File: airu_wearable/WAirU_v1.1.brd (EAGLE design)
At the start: 43.8 x 51.7 mm, 53 parts, among them J2 2p-2.0, Q2 MMBT3904LT1G, Q3 MMBT3904LT1G, Q4 BSS84, Q6 BSS84, U2 CN3065-DFN8, U3 HDC1080DMBT, U4 CJT1117-3.3-SOT223, U6 PAM2401, U7 ESP32_WROOM32_SKINNY

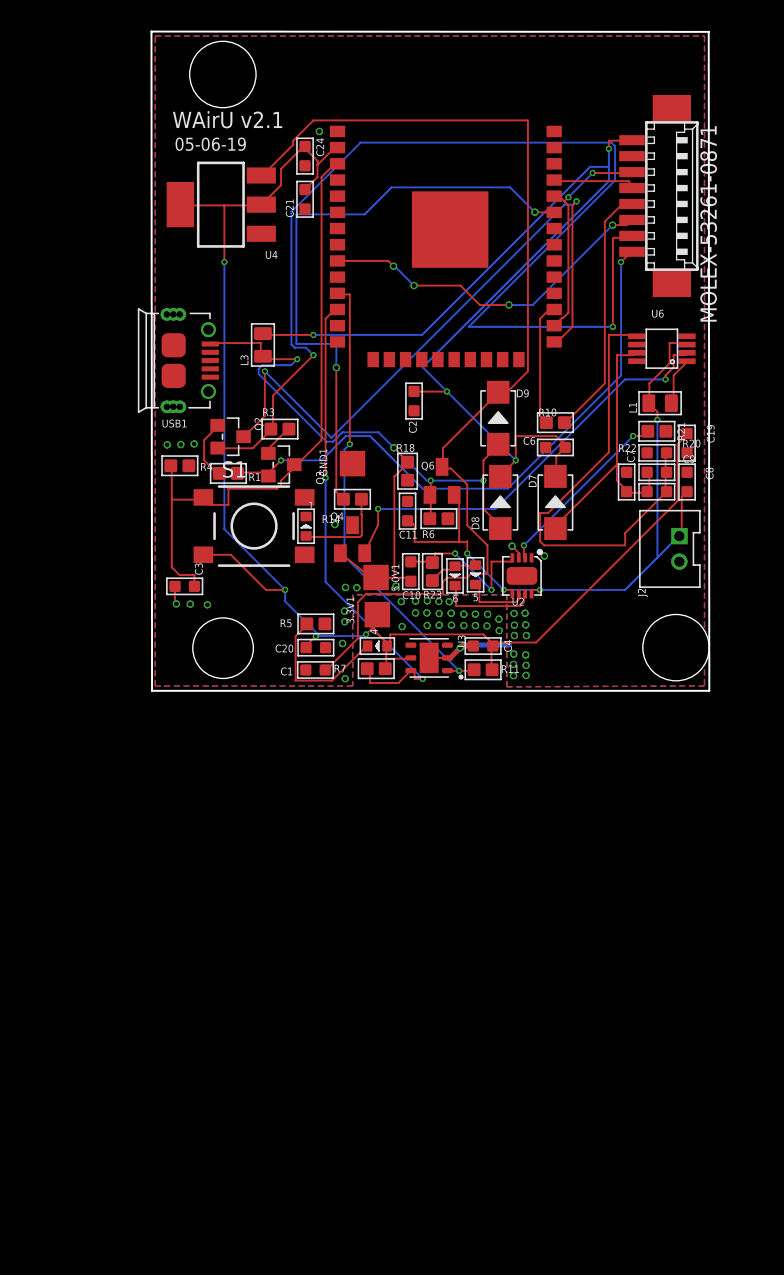
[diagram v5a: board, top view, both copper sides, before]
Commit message: Change regulator, add rules for pads and vias, update new component to BOM sheet
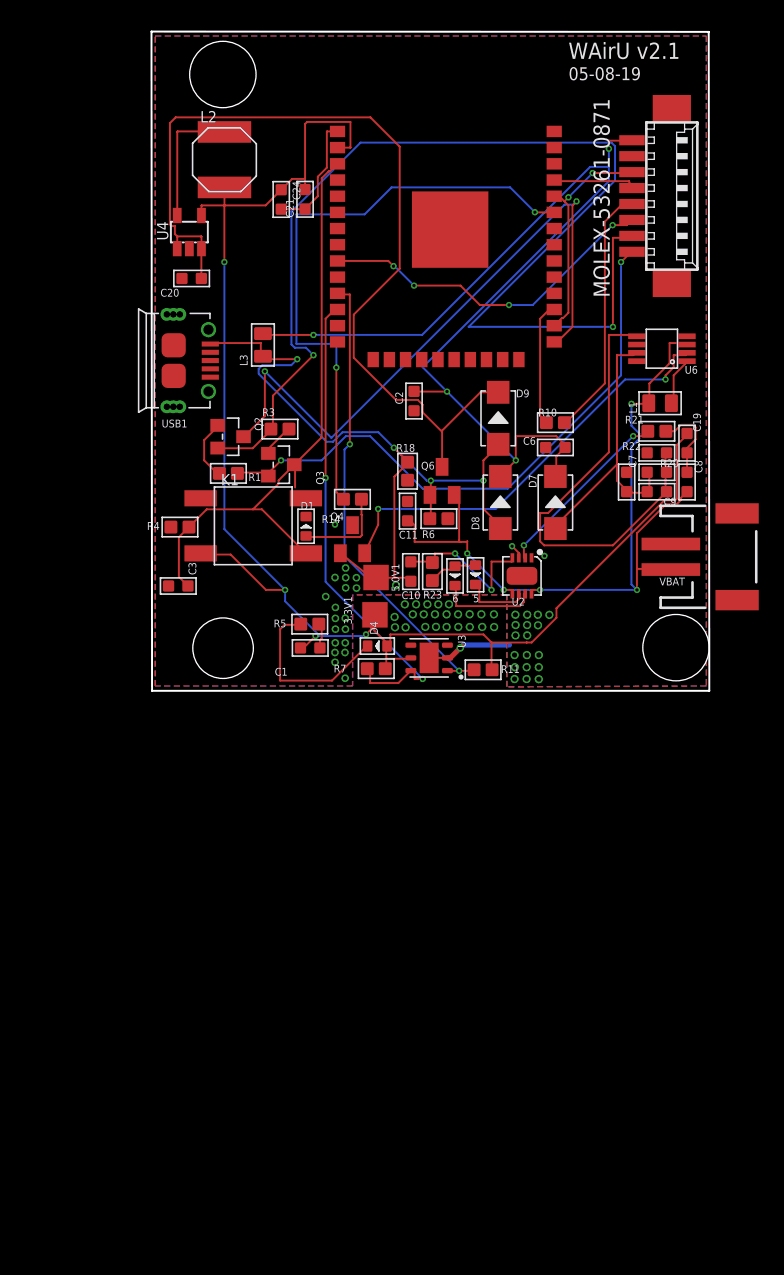
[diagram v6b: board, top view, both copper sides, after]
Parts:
- removed C4: 1uf, Seeed-Capacitor:C0603
- removed GND1: TPTP20SQ, testpad:TP20SQ
- removed J2: 2p-2.0, Seeed-Connector:H2-2.0-6X4.5MM
- removed S1: DTSM-6, switch-tact:DTSM-6
- added K1: (no value), OPL_Switch:SW4-SMD-6.0X6.0X5.0MM
- added L2: 4.7uH, OPL_Inductor:L5040S
- added VBAT: (no value), SparkFun-Connectors:JST-2-SMD
- U4: value CJT1117-3.3-SOT223 -> PAM2305AABADJ; device Seeed-IC:SOT-223 -> OPL_IC:SOT-23-5
- moved C20 32.2 mm to (11.1, 30.8)
- moved R4 4.81 mm to (10.2, 11.3), turned to 90 degrees
- moved C24 3.88 mm to (18.1, 37.0)
- moved U4 3.28 mm to (10.9, 34.4), turned to 0 degrees
- moved C3 0.51 mm to (10.0, 6.66)
- moved R5 0.48 mm to (20.4, 3.66)
- moved C1 0.44 mm to (20.4, 1.80)
- moved 3.3V1 0.19 mm to (25.5, 4.39)
- renumbered 1 to D1, 4 to D4
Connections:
- new net N$75: C20.2, D9.2, Q6.3, U4.1, U4.3
- net 3.3V: now also K1.2, L2.2, U4.4; no longer C4.2, S1.3, U4.2, U4.TER
- net GND: now also U4.2, VBAT.1; no longer C4.1, GND1.TP, J2.-, U4.1
- net N$8: now also L2.1, U4.5; no longer C20.2, D9.2, Q6.3, U4.3
- net RESET: now also K1.3; no longer S1.1
- net VBAT: now also VBAT.2; no longer J2.+
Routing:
- net N$8: track 81.5 -> 10.3 mm
- net N$75: track 0.00 -> 70.8 mm
- net GND: track 10.4 -> 26.3 mm, vias 11 -> 4
- net VBAT: track 55.4 -> 63.5 mm, vias 4 -> 5
- net 3.3V: track 113.2 -> 118.7 mm
- net N$21: track 11.6 -> 14.2 mm
- net N$10: track 36.5 -> 35.9 mm
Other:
- board text added: "05-08-19"
- board text removed: "05-06-19"

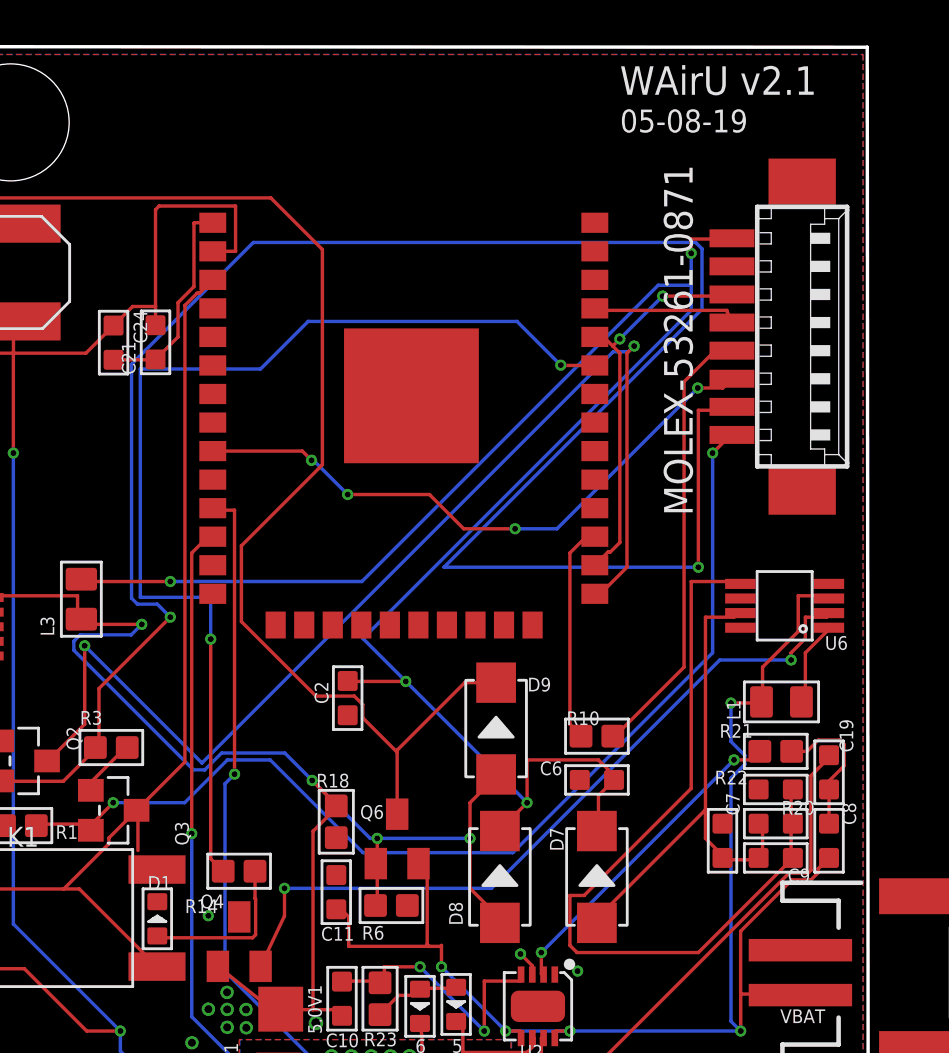
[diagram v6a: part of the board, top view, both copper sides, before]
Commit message: Pull down PM_SET and PM_RESET
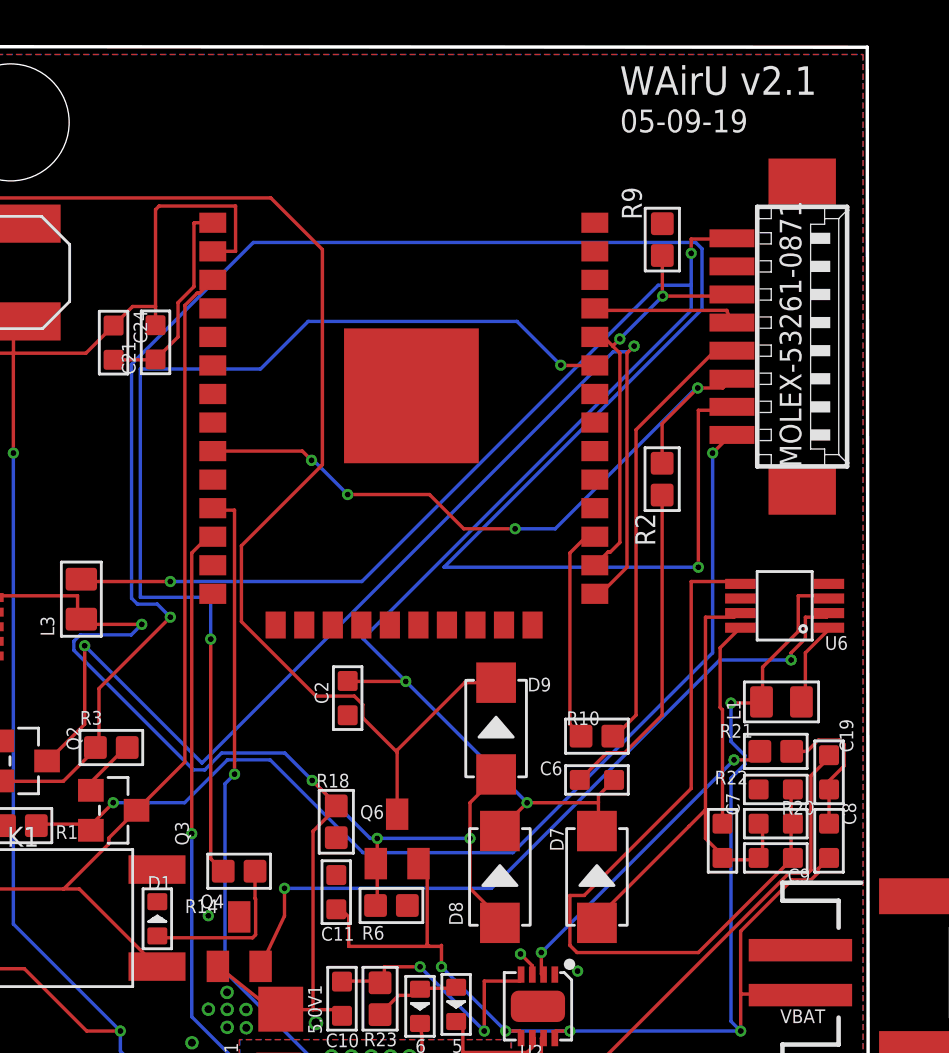
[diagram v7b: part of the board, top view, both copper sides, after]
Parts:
- added R2, R9: 4.7K, Seeed-Resistor:R0603
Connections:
- net GND: now also R2.1, R9.1
- net PM_RESET: now also R2.2
- net PM_SET: now also R9.2
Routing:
- net GND: track 26.3 -> 50.1 mm
- net PM_RESET: track 27.3 -> 31.3 mm
- net 5.0V: track 81.8 -> 79.0 mm
- net RESET: track 48.2 -> 46.3 mm
- net PM_SET: track 17.8 -> 19.6 mm
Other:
- board text added: "05-09-19"
- board text removed: "05-08-19"

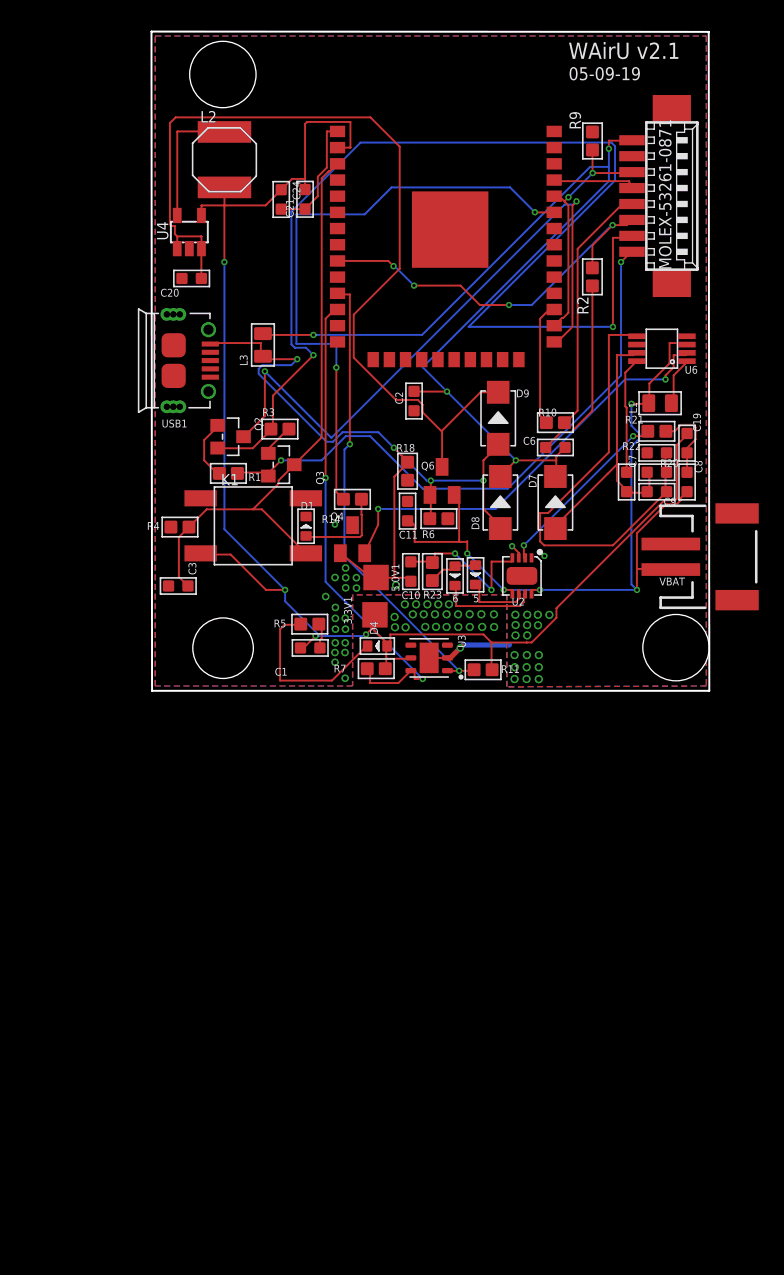
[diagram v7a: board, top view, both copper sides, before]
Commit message: replaced LEDs with single LED, 5V and 3.3V buck/boost are now on the same VIN
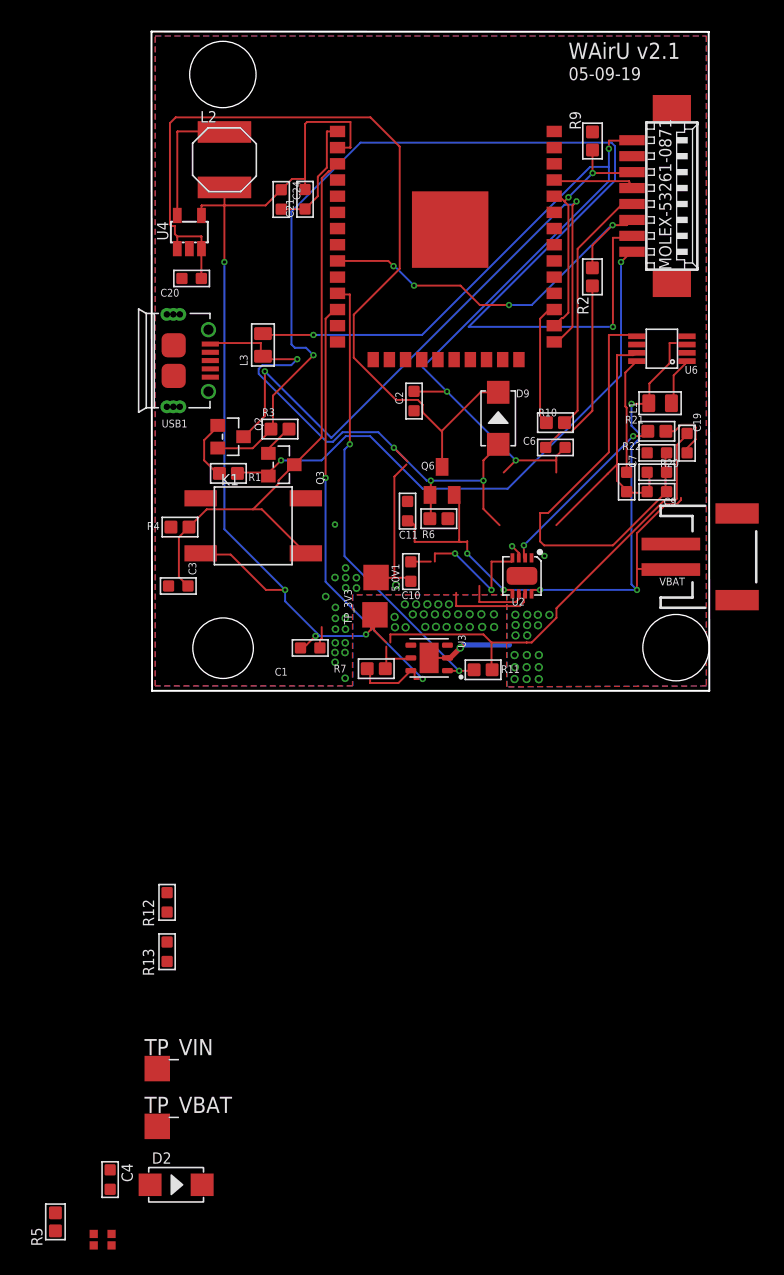
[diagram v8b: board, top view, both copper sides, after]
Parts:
- removed 5: GREEN-0603, Seeed-LED:LED-0603
- removed 6, D1: RED-0603, Seeed-LED:LED-0603
- removed C8: 10uf, OPL_Capacitor:C0603
- removed D4: YELLOW-0603, Seeed-LED:LED-0603
- removed D7, D8: 40V-1A, Seeed-Diode:DO-214AC
- removed Q4: BSS84, BSS84:SOT23
- removed R14: 220R, Seeed-Resistor:R0603
- removed R18: 10K, Seeed-Resistor:R0603
- removed R23: 330R, Seeed-Resistor:R0603
- added C4: 10uf, Seeed-Capacitor:C0603
- added D2: 40V-1A, Seeed-Diode:DO-214AC
- added R12, R13: 100K, OPL_Resistor:R0603
- added TP_VBAT, TP_VIN: TPTP20SQ, testpad:TP20SQ
- added U$4: 19-237A/BHR6GHC-M01/2T, SS_OPL_Unmade:SMD-19-237A
- R5: value 220R -> 330R
- moved R5 51.0 mm to (0.40, -43.2), turned to 0 degrees
- renumbered 3.3V1 to TP_3V3
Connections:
- removed net N$11: 5.+, 6.+, R23.1
- removed net N$14: 5.-, U2.6
- removed net N$21: D4.-, R5.2
- removed net N$23: 6.-, U2.7
- removed net N$7: D1.+, R14.1
- removed net N$75: C20.2, D9.2, Q6.3, U4.1, U4.3
- removed net STAT_LED1: R14.2, U7.33
- removed net STAT_LED2: U7.31
- removed net STAT_LED3: U7.30
- new net BAT_CHECK: R12.2, R13.1, U7.7
- new net CHARGING: U$4.4, U2.7
- new net CHG_DONE: U$4.3, U2.6
- new net GP_LED: U$4.1, U7.16
- new net VBUS_RAW: L3.1, USB1.1
- new net V_IN: C20.2, C4.2, D9.2, L1.1, Q6.3, TP_VIN.TP, U4.1, U4.3, U6.2, U6.3
- net 3.3V: now also R5.2; no longer D4.+
- net 5.0V: now also D2.2; no longer D7.2, D8.2, L3.2
- net GND: now also C4.1, R12.1; no longer C8.1, D1.-, Q4.3, R18.1, R5.1
- net N$4: now also C7.2, C9.2, D2.1, R20.2, U6.7; no longer Q4.2, U6.2
- net N$5: no longer R23.2
- net N$9: now also R5.1, U$4.2; no longer C7.2, C9.2, D7.1, R20.2, U6.7
- net VBAT: now also R13.2, TP_VBAT.TP; no longer C8.2, L1.1, U6.3
- net VBUS: now also L3.2; no longer D8.1, L3.1, Q4.1, R18.2, USB1.1
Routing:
- net V_IN: track 0.00 -> 77.7 mm
- net N$75: track 70.8 -> 0.00 mm
- net STAT_LED1: track 47.6 -> 0.00 mm, vias 2 -> 0
- net N$9: track 23.0 -> 0.00 mm
- net N$21: track 14.2 -> 0.00 mm
- net N$4: track 33.8 -> 22.7 mm, vias 2 -> 0
- net VBUS: track 61.7 -> 52.5 mm
- net VBAT: track 63.5 -> 55.7 mm
- net N$23: track 7.79 -> 0.00 mm
- net N$7: track 7.30 -> 0.00 mm
- net CHARGING: track 0.00 -> 7.22 mm
- net N$14: track 5.30 -> 0.00 mm
- net VBUS_RAW: track 0.00 -> 5.12 mm
- net CHG_DONE: track 0.00 -> 4.98 mm
- net N$11: track 3.92 -> 0.00 mm
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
